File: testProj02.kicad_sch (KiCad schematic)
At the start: 0 parts

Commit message: some changes
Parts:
- added BT1: Battery, symbol Device:Battery
- added C1, C2, C3, C4: C, symbol Device:C
- added C5: C_Polarized, symbol Device:C_Polarized
- added D1, D2: LED, symbol Device:LED
- added H1, H2, H3, H4: MountingHole, symbol Mechanical:MountingHole
- added R1, R2, R3, R4, R5, R6, R7: R, symbol Device:R
- added U1, U2: 24LC1025, symbol Memory_EEPROM:24LC1025
- added U3: DS1337S_, DS1337S_:SOIC127P600X175-8N, symbol DS1337S_:DS1337S_
- added U4: ATMEGA328P-AU, ATMEGA328P-AU:QFP80P900X900X120-32N, symbol ATMEGA328P-AU:ATMEGA328P-AU
- added Y1, Y2: Crystal, symbol Device:Crystal
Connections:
- new net: U4.21 (GND), U4.3 (GND), U4.5 (GND)
- new net: U4.4 (VCC), U4.6 (VCC)
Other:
- added sheet Connectors (connectors.kicad_sch)

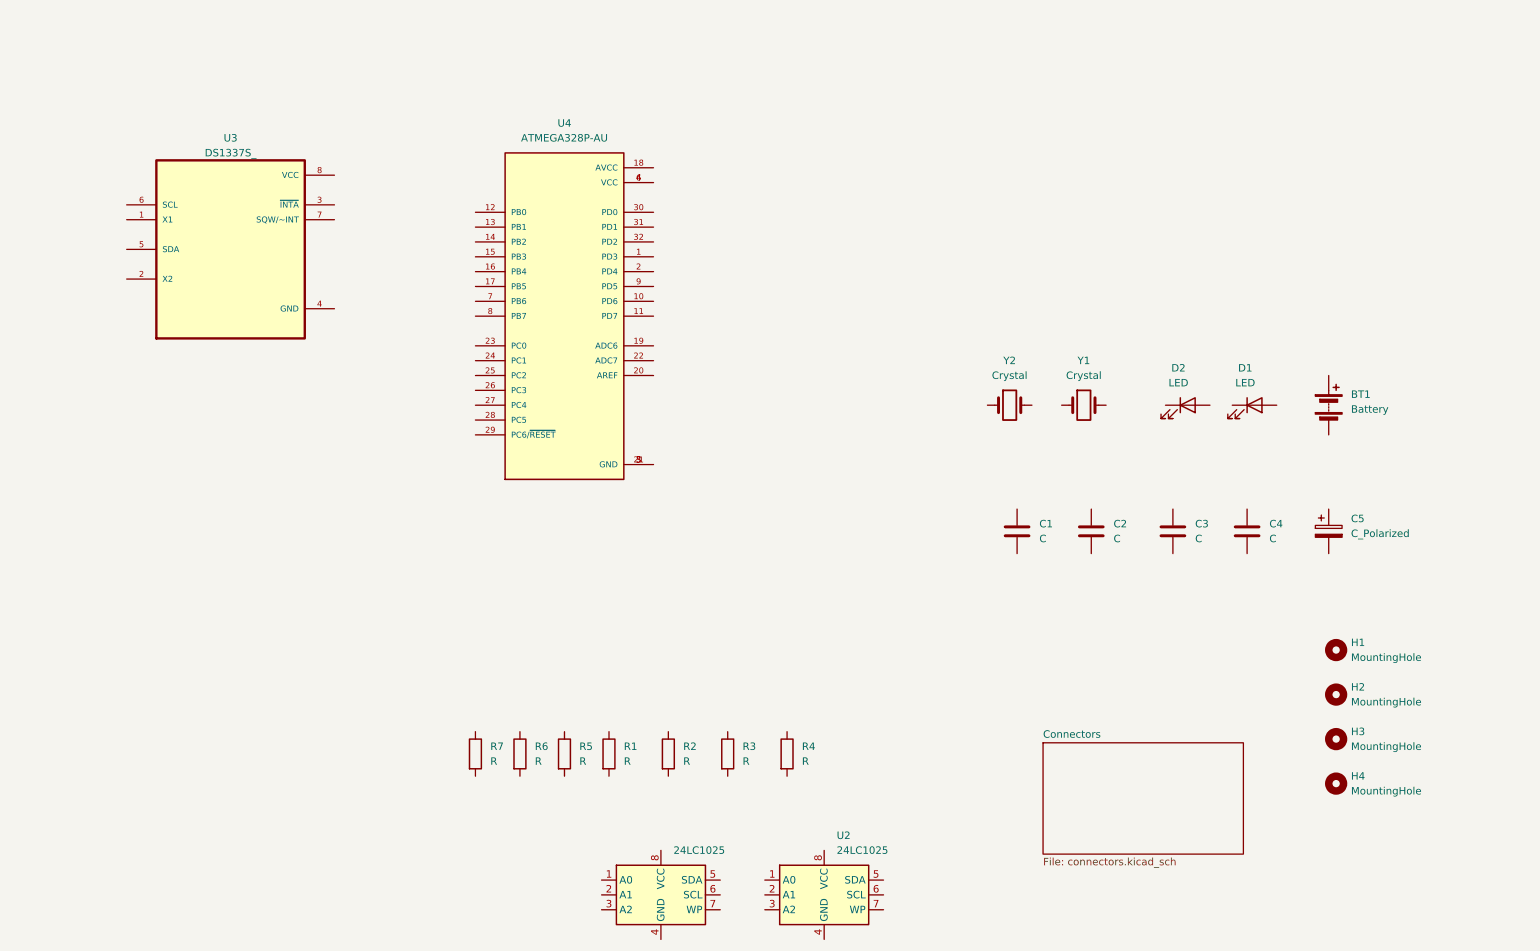
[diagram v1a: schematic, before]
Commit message: Added component values
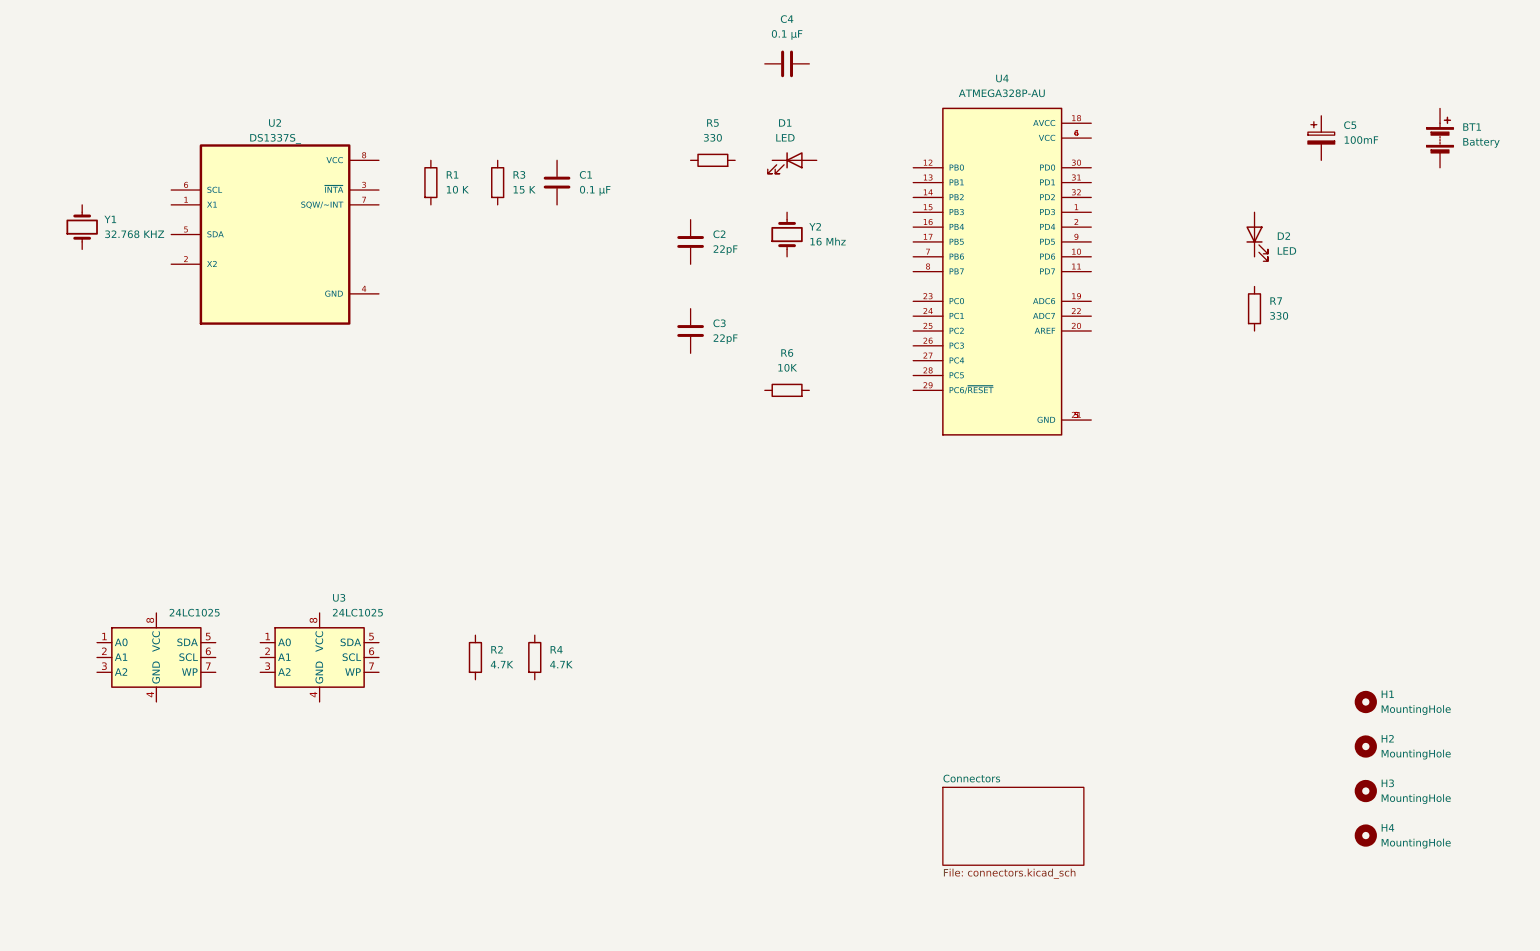
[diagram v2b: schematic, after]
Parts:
- removed R1: R, symbol Device:R
- added R6: 10K, symbol Device:R
- C1: renamed from C3; value C -> 0.1 µF
- C2: renamed from C1; value C -> 22pF
- C3: renamed from C2; value C -> 22pF
- C4: value C -> 0.1 µF
- C5: value C_Polarized -> 100mF
- R1: renamed from R6; value R -> 10 K
- R2: value R -> 4.7K
- R3: renamed from R5; value R -> 15 K
- R4: renamed from R3; value R -> 4.7K
- R5: renamed from R7; value R -> 330
- R7: renamed from R4; value R -> 330
- Y1: renamed from Y2; value Crystal -> 32.768 KHZ
- Y2: renamed from Y1; value Crystal -> 16 Mhz
- renumbered D2 to D1, D1 to D2, U3 to U2, U2 to U3
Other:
- moved on the sheet: BT1, C1, C2, C3, C4, C5, D1, D2, H1, H2, H3, H4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

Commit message: assigned footprints
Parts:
- BT1: footprint (none) -> Connector_PinHeader_2.54mm:PinHeader_1x02_P2.54mm_Vertical
- C1, C2, C3, C4, C5: footprint (none) -> Capacitor_SMD:C_0805_2012Metric
- D1, D2: footprint (none) -> LED_SMD:LED_0805_2012Metric_Pad1.15x1.40mm_HandSolder
- H1, H2, H3, H4: footprint (none) -> MountingHole:MountingHole_2.1mm
- R1, R2, R3, R4, R5, R6, R7: footprint (none) -> Resistor_SMD:R_0805_2012Metric
- U1, U3: footprint (none) -> Package_SO:SOIC-8_5.3x5.3mm_P1.27mm
- U2: footprint DS1337S_:SOIC127P600X175-8N -> Footprints:SOIC127P600X175-8N
- U4: footprint ATMEGA328P-AU:QFP80P900X900X120-32N -> Footprints:QFP80P900X900X120-32N
- Y1, Y2: footprint (none) -> Crystal:Crystal_SMD_5032-2Pin_5.0x3.2mm_HandSoldering
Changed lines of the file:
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@@
 			)
 		)
-		(property "Footprint" ""
+		(property "Footprint" "Resistor_SMD:R_0805_2012Metric"
 			(at 228.092 66.04 90)
 			(effects
@@
 			)
 		)
-		(property "Footprint" ""
+		(property "Footprint" "Capacitor_SMD:C_0805_2012Metric"
 			(at 134.3152 58.42 0)
 			(effects
@@
 			)
 		)
-		(property "Footprint" ""
+		(property "Footprint" "Connector_PinHeader_2.54mm:PinHeader_1x02_P2.54mm_Vertical"
 			(at 261.62 35.306 90)
 			(effects
@@
 			)
 		)
-		(property "Footprint" ""
+		(property "Footprint" "Resistor_SMD:R_0805_2012Metric"
 			(at 137.16 42.418 90)
 			(effects
@@
 			)
 		)
-		(property "Footprint" ""
+		(property "Footprint" "MountingHole:MountingHole_2.1mm"
 			(at 248.92 133.35 0)
 			(effects
@@
 			)
 		)
-		(property "Footprint" ""
+		(property "Footprint" "Capacitor_SMD:C_0805_2012Metric"
 			(at 153.67 23.1648 0)
 			(effects
@@
 			)
 		)
-		(property "Footprint" "DS1337S_:SOIC127P600X175-8N"
+		(property "Footprint" "Footprints:SOIC127P600X175-8N"
 			(at 62.23 53.34 0)
 			(effects
@@
 			)
 		)
-		(property "Footprint" ""
+		(property "Footprint" "Capacitor_SMD:C_0805_2012Metric"
 			(at 111.4552 48.26 0)
 			(effects
@@
 			)
 		)
-		(property "Footprint" ""
+		(property "Footprint" "LED_SMD:LED_0805_2012Metric_Pad1.15x1.40mm_HandSolder"
 			(at 151.13 40.64 0)
 			(effects
@@
 			)
 		)
-		(property "Footprint" ""
+		(property "Footprint" "Crystal:Crystal_SMD_5032-2Pin_5.0x3.2mm_HandSoldering"
 			(at 149.86 53.34 0)
 			(effects
@@
 			)
 		)
-		(property "Footprint" ""
+		(property "Footprint" "Resistor_SMD:R_0805_2012Metric"
 			(at 87.122 44.45 90)
 			(effects
@@
 			)
 		)
-		(property "Footprint" ""
+		(property "Footprint" "LED_SMD:LED_0805_2012Metric_Pad1.15x1.40mm_HandSolder"
 			(at 229.87 53.34 0)
 			(effects
@@
 			)
 		)
-		(property "Footprint" ""
+		(property "Footprint" "MountingHole:MountingHole_2.1mm"
 			(at 248.92 148.59 0)
 			(effects
@@
 			)
 		)
-		(property "Footprint" ""
+		(property "Footprint" "Capacitor_SMD:C_0805_2012Metric"
 			(at 242.2652 40.64 0)
 			(effects
@@
 			)
 		)
-		(property "Footprint" ""
+		(property "Footprint" "Resistor_SMD:R_0805_2012Metric"
 			(at 149.86 81.788 90)
 			(effects
@@
 			)
 		)
-		(property "Footprint" ""
+		(property "Footprint" "Resistor_SMD:R_0805_2012Metric"
 			(at 98.552 44.45 90)
 			(effects
@@
 			)
 		)
-		(property "Footprint" "ATMEGA328P-AU:QFP80P900X900X120-32N"
+		(property "Footprint" "Footprints:QFP80P900X900X120-32N"
 			(at 186.69 59.69 0)
 			(effects
@@
 			)
 		)
-		(property "Footprint" ""
+		(property "Footprint" "MountingHole:MountingHole_2.1mm"
 			(at 248.92 156.21 0)
 			(effects
@@
 			)
 		)
-		(property "Footprint" ""
+		(property "Footprint" "Resistor_SMD:R_0805_2012Metric"
 			(at 104.902 125.73 90)
 			(effects
@@
 			)
 		)
-		(property "Footprint" ""
+		(property "Footprint" "MountingHole:MountingHole_2.1mm"
 			(at 248.92 140.97 0)
 			(effects
@@
 			)
 		)
-		(property "Footprint" ""
+		(property "Footprint" "Package_SO:SOIC-8_5.3x5.3mm_P1.27mm"
 			(at 41.91 125.73 0)
 			(effects
@@
 			)
 		)
-		(property "Footprint" ""
+		(property "Footprint" "Capacitor_SMD:C_0805_2012Metric"
 			(at 134.3152 73.66 0)
 			(effects
@@
 			)
 		)
-		(property "Footprint" ""
+		(property "Footprint" "Crystal:Crystal_SMD_5032-2Pin_5.0x3.2mm_HandSoldering"
 			(at 29.21 52.07 0)
 			(effects
@@
 			)
 		)
-		(property "Footprint" ""
+		(property "Footprint" "Resistor_SMD:R_0805_2012Metric"
 			(at 94.742 125.73 90)
 			(effects
@@
 			)
 		)
-		(property "Footprint" ""
+		(property "Footprint" "Package_SO:SOIC-8_5.3x5.3mm_P1.27mm"
 			(at 69.85 125.73 0)
 			(effects

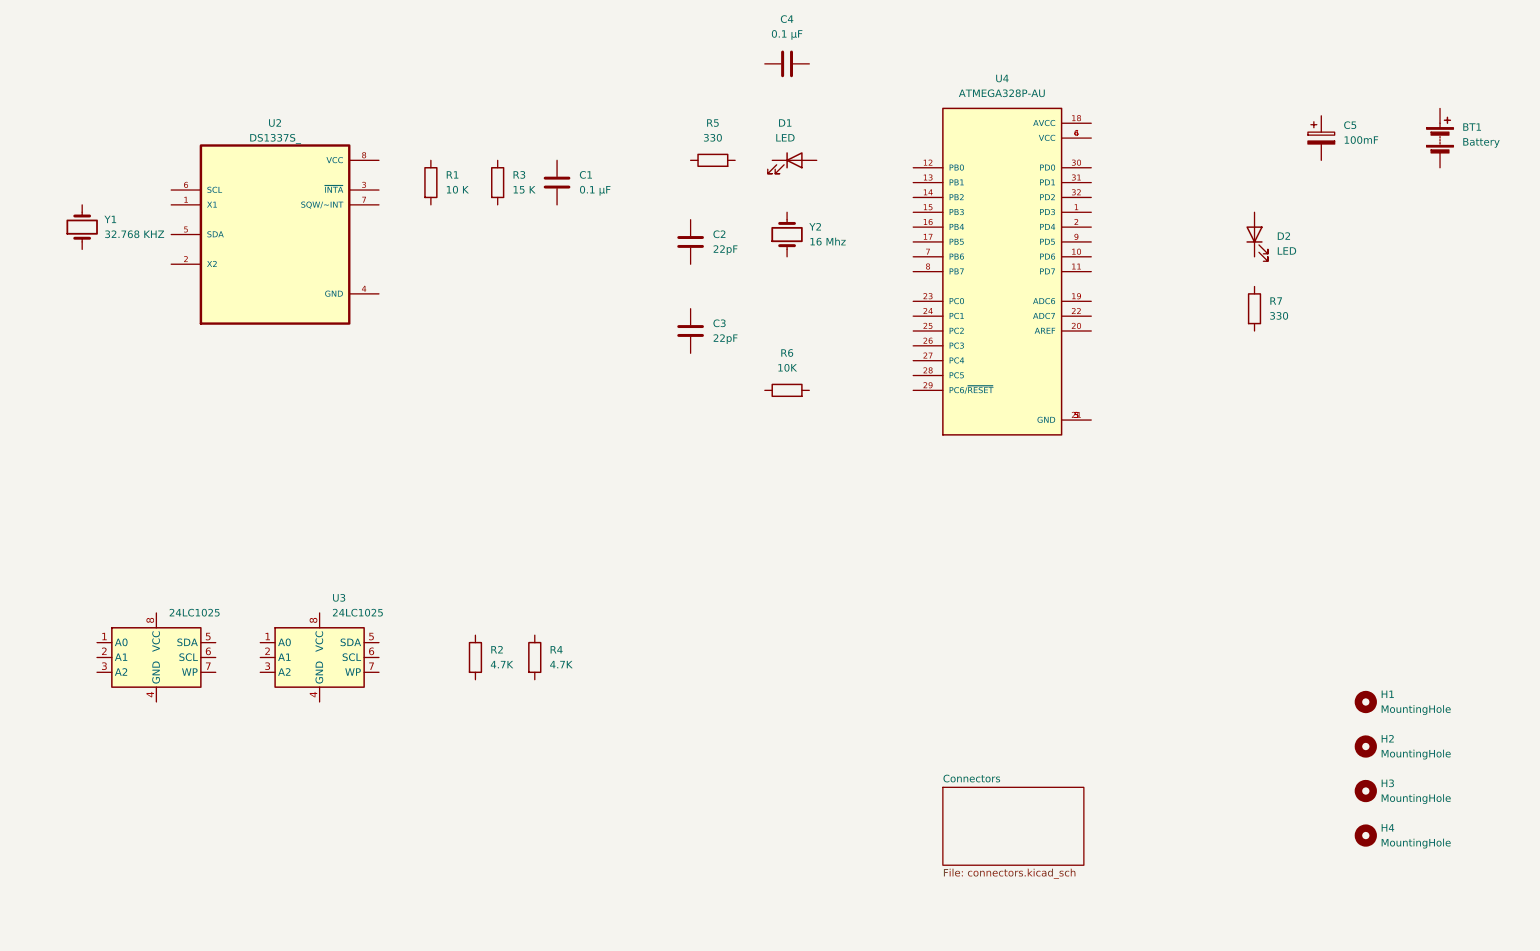
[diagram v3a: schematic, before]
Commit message: Completed Wiring main sheet
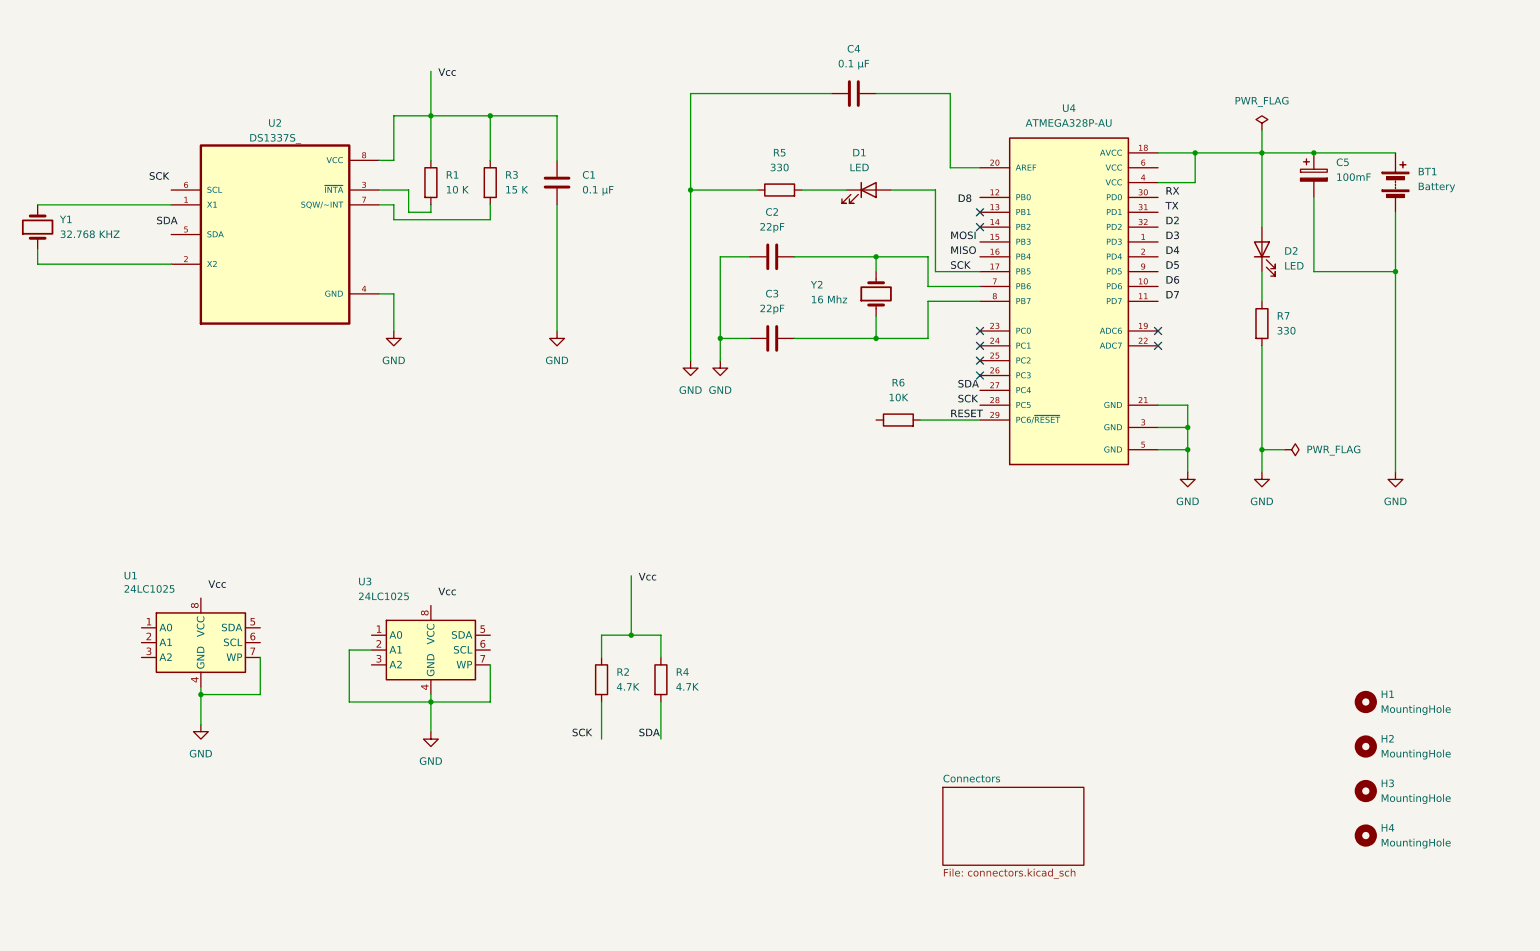
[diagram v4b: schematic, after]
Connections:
- net at R7.1: now also D2.1 (K)
- net GND: now reaches R7.2
- net GND: now also BT1.2 (-), C1.2, C2.1, C3.1, C4.1, C5.2, R5.1, U1.4 (GND), U1.7 (WP), U2.4 (GND), U3.2 (A1), U3.4 (GND), U3.7 (WP), U4.21 (GND), U4.3 (GND), U4.5 (GND)
- net at C2.2: now also U4.7 (PB6), Y2.2
- net at BT1.1 (+): now also C5.1, D2.2 (A), U4.18 (AVCC), U4.4 (VCC)
- net at R5.2: now also D1.1 (K)
- net at C4.2: now also U4.20 (AREF)
- net at U2.1 (X1): now also Y1.2
- net at U2.2 (X2): now also Y1.1
- net at U2.3 (~{INTA}): now also R1.2
- net at U2.7 (SQW/~INT): now also R3.2
- net at U2.8 (VCC): now also C1.1, R1.1, R3.1
- net SCK: now reaches D1.2 (A)
- net SCK: now also U4.17 (PB5)
- net at Y2.1: now also C3.2, U4.8 (PB7)
- net RESET: now reaches R6.2
- net RESET: now also U4.29 (PC6/~{RESET})
- net at U4.6 (VCC): no longer U4.4 (VCC)
- net at R4.1: now also R2.1
- no-connect marks 0 -> 8
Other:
- moved on the sheet: BT1, C2, C3, C4, C5, D1, D2, R2, R3, R4, R5, R6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

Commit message: completed comments
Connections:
- net D2: now also U4.32 (PD2)
- net D3: now also U4.1 (PD3)
- net D4: now also U4.2 (PD4)
- net D5: now also U4.9 (PD5)
- net D6: now also U4.10 (PD6)
- net D7: now also U4.11 (PD7)
- net D8: now also U4.12 (PB0)
- net MISO: now also U4.16 (PB4)
- net MOSI: now also U4.15 (PB3)
- net RX: now also U4.30 (PD0)
- net SCK: now also R2.2, U1.6 (SCL), U2.6 (SCL), U3.6 (SCL), U4.28 (PC5)
- net SDA: now also R4.2, U1.5 (SDA), U2.5 (SDA), U3.5 (SDA), U4.27 (PC4)
- net TX: now also U4.31 (PD1)
- net Vcc: now also C1.1, R1.1, R2.1, R3.1, R4.1, R6.1, U1.1 (A0), U1.2 (A1), U1.3 (A2), U1.8 (VCC), U2.8 (VCC), U3.1 (A0), U3.3 (A2), U3.8 (VCC)
- no-connect marks 8 -> 9
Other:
- sheet Connectors ports: added D2, D3, D4, D5, D6, D7, D8, GND, MISO, MOSI, RESET, RX, SCK, SDA, TX, Vcc; removed none
- note added: "EEPROM"
- note added: "MCU"
- note added: "Mounting"
- note added: "Real Time Clock"
- moved on the sheet: BT1, C2, C3, C4, C5, D1, D2, H1, H2, H3, H4, R2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
